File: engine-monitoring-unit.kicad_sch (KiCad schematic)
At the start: 58 parts, among them J1 Conn_01x04_Pin, J2 Supply, J3 Oil Temperature, J4 Air Temperature, J5 Air Temperature, J7 Inductive Sensor Wire, Q1 2N3904, SW1 KEY, SW2 RST, SW3 BOOT, U1 STM32F411CEU6, U2 LMR16006XDDCR, Y1 LSE, Y3 HSE

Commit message: Assigned Footprints for components
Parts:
- removed C5: C, symbol Device:C
- removed J7: Inductive Sensor Wire, TerminalBlock_Phoenix:TerminalBlock_Phoenix_MKDS-1,5-2-5.08_1x02_P5.08mm_Horizontal, symbol Connector:Screw_Terminal_01x02
- removed L1: L, symbol Device:L
- added C4: 100nF, Capacitor_SMD:C_0603_1608Metric_Pad1.08x0.95mm_HandSolder, symbol Device:C
- added J6: Sense Wire, Connector_Molex:Molex_Micro-Fit_3.0_43650-0200_1x02_P3.00mm_Horizontal, symbol Connector:Conn_01x02_Socket
- C1: renamed from C2; value C -> 4.7uF; footprint (none) -> Capacitor_SMD:C_0603_1608Metric_Pad1.08x0.95mm_HandSolder
- C10: renamed from C13; footprint (none) -> Capacitor_SMD:C_0603_1608Metric_Pad1.08x0.95mm_HandSolder
- C11: renamed from C9; value C -> 6.8pF; footprint (none) -> Capacitor_SMD:C_0603_1608Metric_Pad1.08x0.95mm_HandSolder
- C12: renamed from C15; footprint (none) -> Capacitor_SMD:C_0603_1608Metric_Pad1.08x0.95mm_HandSolder
- C13: renamed from C10; value C -> 6.8pF; footprint (none) -> Capacitor_SMD:C_0603_1608Metric_Pad1.08x0.95mm_HandSolder
- C14: renamed from C6; value C -> 4.7uF; footprint (none) -> Capacitor_SMD:C_0603_1608Metric_Pad1.08x0.95mm_HandSolder
- C15: renamed from C17; footprint (none) -> Capacitor_SMD:C_0603_1608Metric_Pad1.08x0.95mm_HandSolder
- C16: footprint (none) -> Capacitor_SMD:C_0603_1608Metric_Pad1.08x0.95mm_HandSolder
- C17: renamed from C14; footprint Capacitor_THT:CP_Radial_D8.0mm_P3.50mm -> Capacitor_SMD:C_0603_1608Metric_Pad1.08x0.95mm_HandSolder
- C2: renamed from C3; value C -> 100nF; footprint (none) -> Capacitor_SMD:C_0603_1608Metric_Pad1.08x0.95mm_HandSolder
- C3: renamed from C4; value C -> 100nF; footprint (none) -> Capacitor_SMD:C_0603_1608Metric_Pad1.08x0.95mm_HandSolder
- C5: renamed from C1; footprint (none) -> Capacitor_SMD:C_0603_1608Metric_Pad1.08x0.95mm_HandSolder
- C6: renamed from C7; value C -> 24pF; footprint (none) -> Capacitor_SMD:C_0603_1608Metric_Pad1.08x0.95mm_HandSolder
- C7: renamed from C11; footprint (none) -> Capacitor_SMD:C_0603_1608Metric_Pad1.08x0.95mm_HandSolder
- C8: renamed from C12; value 2.2uF -> 4.7uF; footprint (none) -> Capacitor_SMD:C_0603_1608Metric_Pad1.08x0.95mm_HandSolder
- C9: renamed from C8; value C -> 24pF; footprint (none) -> Capacitor_SMD:C_0603_1608Metric_Pad1.08x0.95mm_HandSolder
- D1: renamed from D2; footprint (none) -> LED_SMD:LED_0603_1608Metric_Pad1.05x0.95mm_HandSolder
- D2: renamed from D1; footprint (none) -> LED_SMD:LED_0603_1608Metric_Pad1.05x0.95mm_HandSolder
- J1: value Conn_01x04_Pin -> SW Debug; footprint (none) -> Connector_PinHeader_1.00mm:PinHeader_1x04_P1.00mm_Vertical
- J2, J3, J4: footprint (none) -> Connector_Molex:Molex_Micro-Fit_3.0_43650-0200_1x02_P3.00mm_Horizontal
- J5: value Air Temperature -> Wheel Speed; footprint (none) -> Connector_Molex:Molex_Micro-Fit_3.0_43650-0200_1x02_P3.00mm_Horizontal
- R1: renamed from R4; value R -> 1K; footprint (none) -> Resistor_SMD:R_0603_1608Metric_Pad0.98x0.95mm_HandSolder
- R10: renamed from R13; footprint (none) -> Resistor_SMD:R_0603_1608Metric_Pad0.98x0.95mm_HandSolder
- R11: renamed from R14; footprint (none) -> Resistor_SMD:R_0603_1608Metric_Pad0.98x0.95mm_HandSolder
- R13: renamed from R12; footprint Resistor_THT:R_Axial_DIN0207_L6.3mm_D2.5mm_P10.16mm_Horizontal -> Resistor_SMD:R_0603_1608Metric_Pad0.98x0.95mm_HandSolder
- R15: renamed from R10; footprint Resistor_THT:R_Axial_DIN0207_L6.3mm_D2.5mm_P10.16mm_Horizontal -> Resistor_SMD:R_0603_1608Metric_Pad0.98x0.95mm_HandSolder
- R16: renamed from R11; footprint Resistor_THT:R_Axial_DIN0207_L6.3mm_D2.5mm_P10.16mm_Horizontal -> Resistor_SMD:R_0603_1608Metric_Pad0.98x0.95mm_HandSolder
- R2: renamed from R3; footprint (none) -> Resistor_SMD:R_0603_1608Metric_Pad0.98x0.95mm_HandSolder
- R3: renamed from R2; footprint (none) -> Resistor_SMD:R_0603_1608Metric_Pad0.98x0.95mm_HandSolder
- R4: renamed from R5; value R -> 1K; footprint (none) -> Resistor_SMD:R_0603_1608Metric_Pad0.98x0.95mm_HandSolder
- R5: renamed from R1; footprint (none) -> Resistor_SMD:R_0603_1608Metric_Pad0.98x0.95mm_HandSolder
- R6, R7: footprint (none) -> Resistor_SMD:R_0603_1608Metric_Pad0.98x0.95mm_HandSolder
- R8: renamed from R9; footprint (none) -> Resistor_SMD:R_0603_1608Metric_Pad0.98x0.95mm_HandSolder
- R9: renamed from R8; footprint (none) -> Resistor_SMD:R_0603_1608Metric_Pad0.98x0.95mm_HandSolder
- SW1: footprint (none) -> Button_Switch_SMD:SW_Push_SPST_NO_Alps_SKRK
- SW2: renamed from SW3; footprint (none) -> Button_Switch_SMD:SW_Push_SPST_NO_Alps_SKRK
- SW3: renamed from SW2; footprint (none) -> Button_Switch_SMD:SW_Push_SPST_NO_Alps_SKRK
- renumbered D5 to D4, D4 to D5, L2 to L1, R18 to R12, R17 to R14, R15 to R17, R16 to R18, U2 to U1, U1 to U2, Y3 to Y1, Y1 to Y2
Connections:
- net +3.3V: now also C1.1, C2.1, C3.1, U2.9 (VDDA), C4.1
- net GND: now also C4.2, J6.2 (Pin_2)
- net at D5.2 (A), D7.1 (K): now also J6.1 (Pin_1)
- no-connect marks 0 -> 24
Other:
- note added: "0603"
- note added: "CAPS 0603/16v HSE - 8MHz LSE - 32.768KHz"
- note added: "DONE"
- moved on the sheet: C1, C3

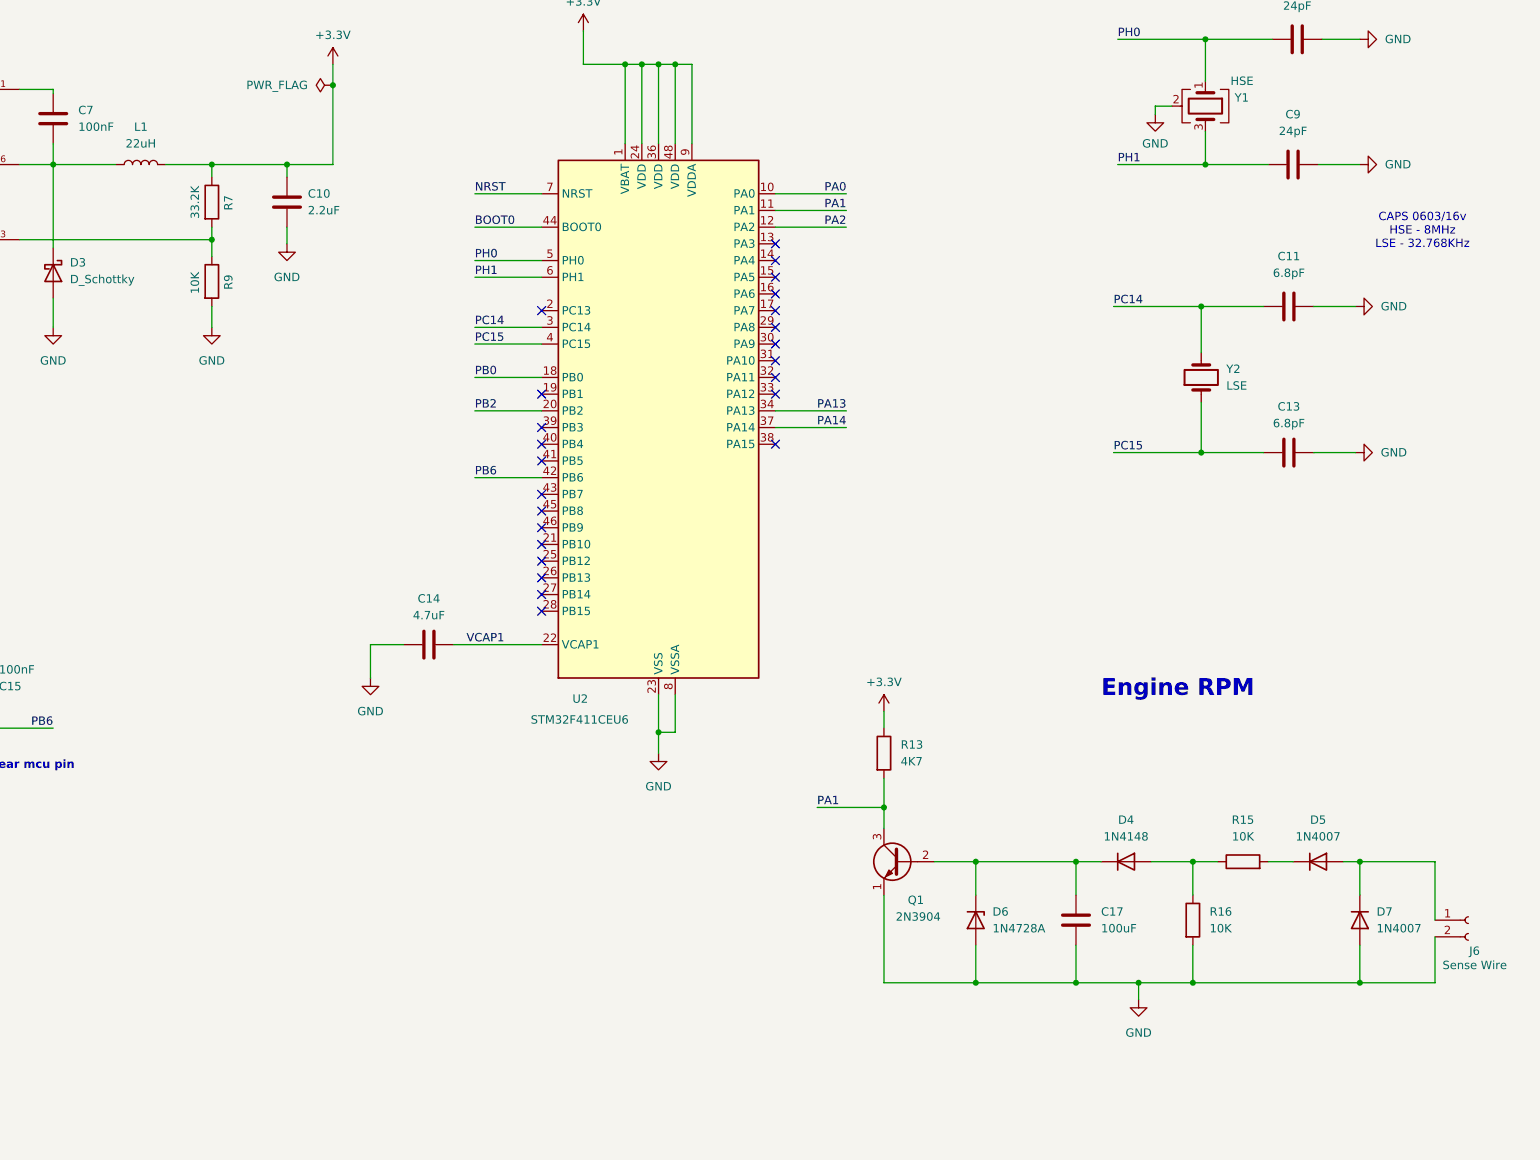
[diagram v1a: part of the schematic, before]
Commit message: Assigned 3D Models for missing ones
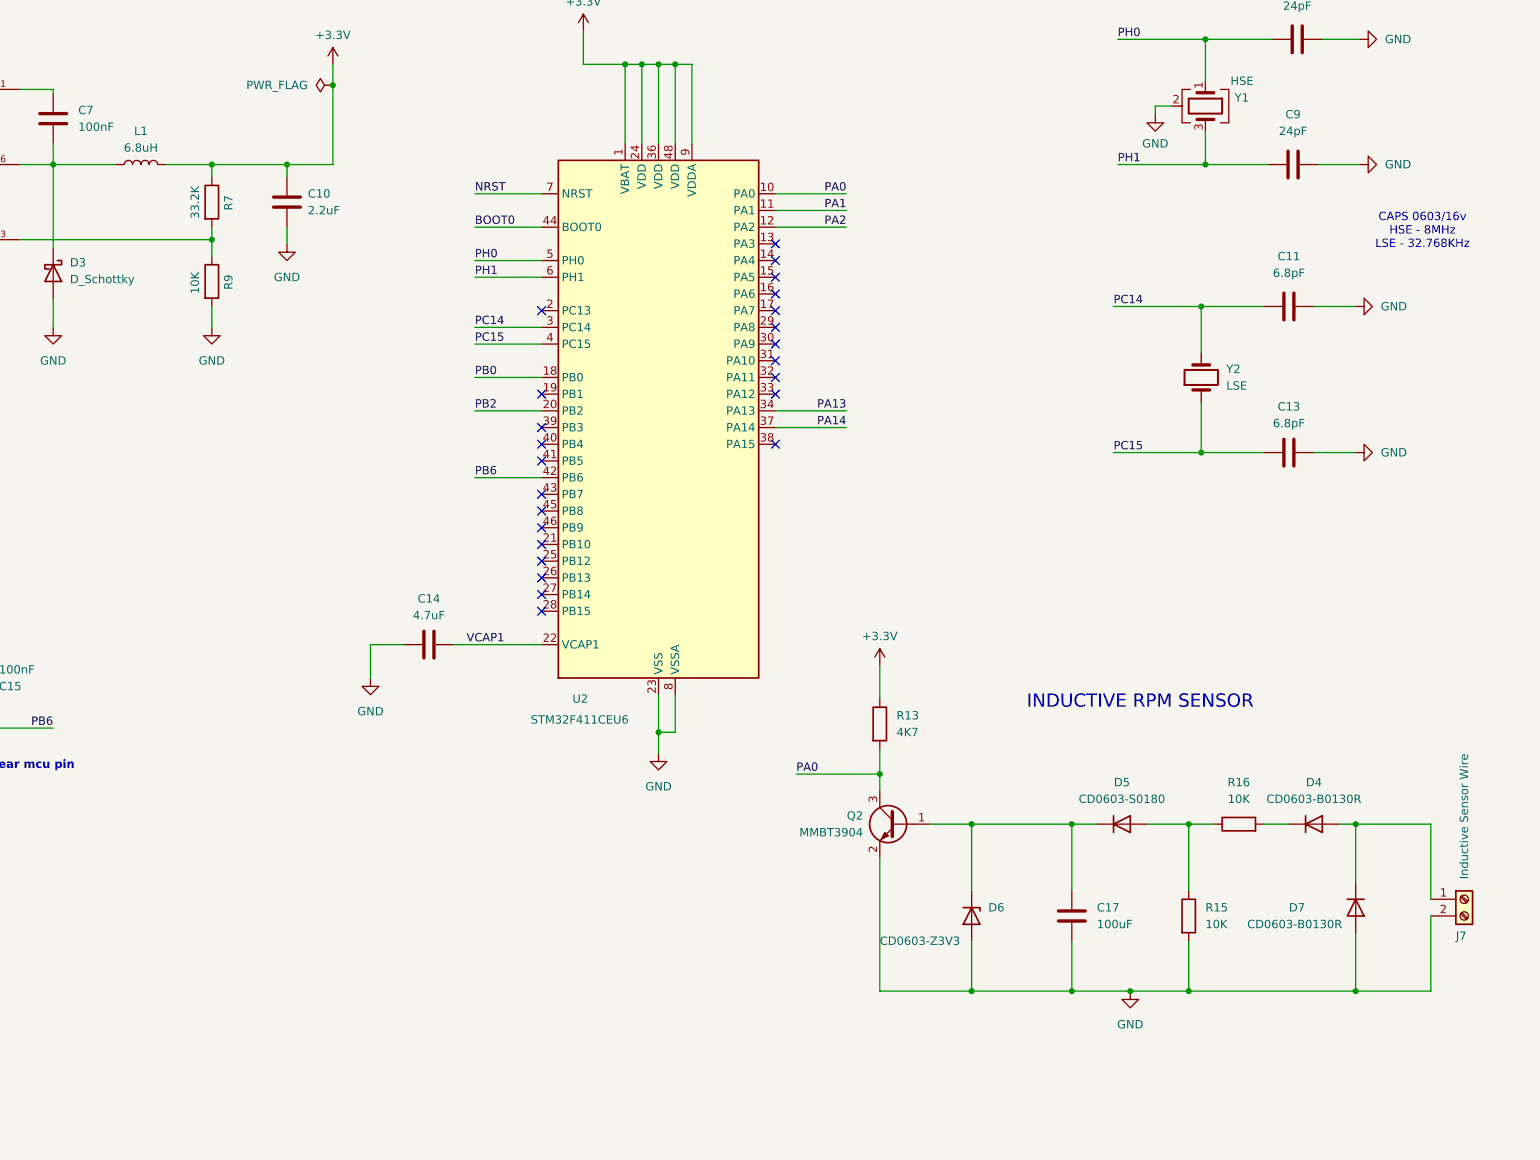
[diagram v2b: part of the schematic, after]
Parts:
- removed D4: 1N4148, Diode_THT:D_DO-35_SOD27_P7.62mm_Horizontal, symbol Diode:1N4148
- removed D5: 1N4007, Diode_THT:D_DO-41_SOD81_P10.16mm_Horizontal, symbol Diode:1N4007
- removed J6: Sense Wire, Connector_Molex:Molex_Micro-Fit_3.0_43650-0200_1x02_P3.00mm_Horizontal, symbol Connector:Conn_01x02_Socket
- removed Q1: 2N3904, Package_TO_SOT_THT:TO-92_Inline, symbol Transistor_BJT:2N3904
- added D4: CD0603-B0130R, Diode_SMD:D_0603_1608Metric_Pad1.05x0.95mm_HandSolder, symbol Diode:1N4007
- added D5: CD0603-S0180, Diode_SMD:D_0603_1608Metric_Pad1.05x0.95mm_HandSolder, symbol Diode:1N4148
- added J7: Inductive Sensor Wire, Connector_Molex:Molex_Micro-Fit_3.0_43650-0200_1x02_P3.00mm_Horizontal, symbol Connector:Screw_Terminal_01x02
- added Q2: MMBT3904, Package_TO_SOT_SMD:SOT-23, symbol Transistor_BJT:MMBT3904
- D3: footprint (none) -> Schottky:POWERDI-123_L2_8-W1_8-LS3_7-RD-1_SS14FP_C894423
- D6: value 1N4728A -> CD0603-Z3V3; footprint Diode_THT:D_DO-41_SOD81_P10.16mm_Horizontal -> Diode_SMD:D_0603_1608Metric_Pad1.05x0.95mm_HandSolder
- D7: value 1N4007 -> CD0603-B0130R; footprint Diode_THT:D_DO-41_SOD81_P10.16mm_Horizontal -> Diode_SMD:D_0603_1608Metric_Pad1.05x0.95mm_HandSolder
- L1: value 22uH -> 6.8uH; footprint (none) -> Inductor-6.8uH:IND-SMD_L4_0-W4_0_NRS4018T_NRS4018T6R8MDGJ_C222881
- R12, R14, R17, R18: footprint Resistor_THT:R_Axial_DIN0207_L6.3mm_D2.5mm_P10.16mm_Horizontal -> Resistor_SMD:R_0603_1608Metric_Pad0.98x0.95mm_HandSolder
- Y1: footprint (none) -> CRYSTAL-SMD_4P-L3_2-W2_5-BL_0132M4-8_000F16DTNJL_C19674293:CRYSTAL-SMD_4P-L3_2-W2_5-BL_0132M4-8_000F16DTNJL_C19674293
- Y2: footprint (none) -> lse:CRYSTAL-SMD_L3_2-W1_5-1_3131M32768DT06LL_C5221300
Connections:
- net GND: now also R15.2, J7.2 (Pin_2), Q2.2 (E); no longer R16.2
- net PA0: now also R13.2, Q2.3 (C)
- net PA1: no longer R13.2
- net at D7.1 (K): now also D4.2 (A), J7.1 (Pin_1)
- net at C17.1, D6.1 (K): now also D5.1 (K), Q2.1 (B)
- net at R15.1, R16.1: now also D5.2 (A)
- new net: D4.1 (K), R16.2
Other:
- note added: "INDUCTIVE RPM SENSOR"
- note removed: "Engine RPM"

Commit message: Updated Page Settings, Board Stackup and Constraints
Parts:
- renumbered D5 to D4, D4 to D5, D7 to D6, D6 to D7, J7 to J6, Q2 to Q1, R16 to R15, R15 to R16
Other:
- title: (none) -> Engine Monitoring Unit
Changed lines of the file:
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@@
 	(generator_version "10.0")
 	(paper "A3")
+	(title_block
+		(title "Engine Monitoring Unit")
+		(date "2026-08-05")
+		(rev "V1.0")
+		(comment 1 "Designed By - Harsha ")
+	)
 	(text "Indicator LEDs\n"
 		(exclude_from_sim no)
@@
 		)
 	)
+	(text "DONE\n"
+		(exclude_from_sim no)
+		(at 377.19 199.39 0)
+		(effects
+			(font
+				(size 1.27 1.27)
+				(thickness 0.254)
+				(bold yes)
+			)
+		)
+	)
 	(text "Place Cap near mcu pin\n"
 		(exclude_from_sim no)
@@
 		(effects
 			(font
-				(size 2.032 2.032)
+				(size 2.54 2.54)
+				(thickness 0.508)
+				(bold yes)
 			)
 		)
@@
 		(dnp no)
 		(fields_autoplaced yes)
-		(property "Reference" "#PWR041"
+		(property "Reference" "#PWR035"
 			(at 309.88 196.85 0)
 			(hide yes)
@@
 			(project "engine-monitoring-unit"
 				(path "/a9d3b11f-88d8-4654-952a-404ab772bc93"
-					(reference "#PWR041")
+					(reference "#PWR035")
 					(unit 1)
 				)
@@
 		(in_pos_files yes)
 		(dnp no)
-		(property "Reference" "Q2"
+		(property "Reference" "Q1"
 			(at 307.34 215.8999 0)
 			(show_name no)
@@
 			(project "engine-monitoring-unit"
 				(path "/a9d3b11f-88d8-4654-952a-404ab772bc93"
-					(reference "Q2")
+					(reference "Q1")
 					(unit 1)
 				)
@@
 		(in_pos_files yes)
 		(dnp no)
-		(property "Reference" "D7"
+		(property "Reference" "D6"
 			(at 372.11 229.8699 90)
 			(show_name no)
@@
 			(project "engine-monitoring-unit"
 				(path "/a9d3b11f-88d8-4654-952a-404ab772bc93"
-					(reference "D7")
+					(reference "D6")
 					(unit 1)
 				)
@@
 		(dnp no)
 		(fields_autoplaced yes)
-		(property "Reference" "#PWR036"
+		(property "Reference" "#PWR041"
 			(at 347.98 248.92 0)
 			(hide yes)
@@
 			(project "engine-monitoring-unit"
 				(path "/a9d3b11f-88d8-4654-952a-404ab772bc93"
-					(reference "#PWR036")
+					(reference "#PWR041")
 					(unit 1)
 				)
@@
 		(dnp no)
 		(fields_autoplaced yes)
-		(property "Reference" "D5"
+		(property "Reference" "D4"
 			(at 346.71 210.82 0)
 			(show_name no)
@@
 			(project "engine-monitoring-unit"
 				(path "/a9d3b11f-88d8-4654-952a-404ab772bc93"
-					(reference "D5")
+					(reference "D4")
 					(unit 1)
 				)
@@
 		(in_pos_files yes)
 		(dnp no)
-		(property "Reference" "D6"
+		(property "Reference" "D7"
 			(at 326.39 229.8699 90)
 			(show_name no)
@@
 			(project "engine-monitoring-unit"
 				(path "/a9d3b11f-88d8-4654-952a-404ab772bc93"
-					(reference "D6")
+					(reference "D7")
 					(unit 1)
 				)
@@
 		(dnp no)
 		(fields_autoplaced yes)
-		(property "Reference" "#PWR035"
+		(property "Reference" "#PWR036"
 			(at 232.41 201.295 0)
 			(hide yes)
@@
 			(project "engine-monitoring-unit"
 				(path "/a9d3b11f-88d8-4654-952a-404ab772bc93"
-					(reference "#PWR035")
+					(reference "#PWR036")
 					(unit 1)
 				)
@@
 		(dnp no)
 		(fields_autoplaced yes)
-		(property "Reference" "R15"
+		(property "Reference" "R16"
 			(at 359.41 229.8699 0)
 			(show_name no)
@@
 			(project "engine-monitoring-unit"
 				(path "/a9d3b11f-88d8-4654-952a-404ab772bc93"
-					(reference "R15")
+					(reference "R16")
 					(unit 1)
 				)
@@
 		(dnp no)
 		(fields_autoplaced yes)
-		(property "Reference" "D4"
+		(property "Reference" "D5"
 			(at 375.92 210.82 0)
 			(show_name no)
@@
 			(project "engine-monitoring-unit"
 				(path "/a9d3b11f-88d8-4654-952a-404ab772bc93"
-					(reference "D4")
+					(reference "D5")
 					(unit 1)
 				)
@@
 		(dnp no)
 		(fields_autoplaced yes)
-		(property "Reference" "R16"
+		(property "Reference" "R15"
 			(at 364.49 210.82 90)
 			(show_name no)
@@
 			(project "engine-monitoring-unit"
 				(path "/a9d3b11f-88d8-4654-952a-404ab772bc93"
-					(reference "R16")
+					(reference "R15")
 					(unit 1)
 				)
@@
 		(in_pos_files yes)
 		(dnp no)
-		(property "Reference" "J7"
+		(property "Reference" "J6"
 			(at 397.51 234.188 0)
 			(show_name no)
@@
 			(project "engine-monitoring-unit"
 				(path "/a9d3b11f-88d8-4654-952a-404ab772bc93"
-					(reference "J7")
+					(reference "J6")
 					(unit 1)
 				)

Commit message: Layed out decoupling caps, connectors and switches
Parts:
- removed C14: 4.7uF, Capacitor_SMD:C_0603_1608Metric_Pad1.08x0.95mm_HandSolder, symbol Device:C
- added C1, C6, C7: 100nF, Capacitor_SMD:C_0603_1608Metric_Pad1.08x0.95mm_HandSolder, symbol Device:C
- added C17: 4.7uF, Capacitor_SMD:C_0603_1608Metric_Pad1.08x0.95mm_HandSolder, symbol Device:C
- D1: value LED_PWR -> LED_USER
- D2: value LED_USER -> LED_PWR
- renumbered C7 to C10, C8 to C11, C9 to C12, C10 to C13, C11 to C14, C12 to C15, C13 to C16, C15 to C18, C16 to C19, C1 to C2, C17 to C20, C2 to C3, C3 to C4, C4 to C5, C5 to C8, C6 to C9
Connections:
- net +3.3V: now also C6.1, C7.1
- net GND: now also C1.1, C17.1, C6.2, C7.2
- net PA0: now also C1.2
- net PA3: now also U2.13 (PA3)
- net PC13: now also U2.2 (PC13)
- net VCAP1: now also C17.2
- net PA1: no longer names the net of U2.11 (PA1)
- no-connect marks 24 -> 23

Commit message: Routed Signal Traces
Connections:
- net PA0: no longer C1.2, SW1.1
- net PA11: now reaches U2.32 (PA11)
- net PA11: now also C1.2, SW1.1
- no-connect marks 23 -> 22
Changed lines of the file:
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@@
+	)
+	(junction
+		(at 234.95 49.53)
+		(diameter 0)
+		(color 0 0 0 0)
+	)
+	(junction
+		(at 141.605 105.41)
+		(diameter 0)
+		(color 0 0 0 0)
+	)
+	(junction
+		(at 182.88 50.165)
+		(diameter 0)
+		(color 0 0 0 0)
 	)
 	(junction
@@
 	)
 	(junction
-		(at 234.95 49.53)
-		(diameter 0)
-		(color 0 0 0 0)
-	)
-	(junction
-		(at 141.605 105.41)
-		(diameter 0)
-		(color 0 0 0 0)
-	)
-	(junction
-		(at 182.88 50.165)
-		(diameter 0)
-		(color 0 0 0 0)
-	)
-	(junction
 		(at 123.19 100.965)
 		(diameter 0)
@@
 		(diameter 0)
 		(color 0 0 0 0)
-	)
-	(no_connect
-		(at 297.18 148.59)
 	)
 	(no_connect
@@
 	(wire
 		(pts
+			(xy 297.18 148.59) (xy 307.34 148.59)
+		)
+		(stroke
+			(width 0)
+			(type default)
+		)
+	)
+	(wire
+		(pts
 			(xy 141.605 114.3) (xy 141.605 116.84)
 		)
@@
 	(wire
 		(pts
+			(xy 31.75 34.29) (xy 36.83 34.29)
+		)
+		(stroke
+			(width 0)
+			(type default)
+		)
+	)
+	(wire
+		(pts
 			(xy 375.92 160.655) (xy 382.27 160.655)
 		)
@@
 		(pts
 			(xy 267.97 95.885) (xy 267.97 100.965)
-		)
-		(stroke
-			(width 0)
-			(type default)
-		)
-	)
-	(wire
-		(pts
-			(xy 33.655 34.29) (xy 36.83 34.29)
 		)
 		(stroke
@@
 		)
 	)
+	(label "PA11"
+		(at 31.75 34.29 180)
+		(effects
+			(font
+				(size 1.27 1.27)
+				(thickness 0.1588)
+			)
+			(justify right bottom)
+		)
+	)
 	(label "PA2"
 		(at 307.975 125.73 180)
@@
 		)
 	)
-	(label "PA0"
-		(at 33.655 34.29 0)
+	(label "PA11"
+		(at 307.34 148.59 180)
 		(effects
 			(font
 				(size 1.27 1.27)
+				(thickness 0.1588)
 			)
-			(justify left bottom)
-		)
-	)
+			(justify right bottom)
+		)
+	)

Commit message: Updated Footprint for swd
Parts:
- J1: footprint Connector_PinHeader_1.00mm:PinHeader_1x04_P1.00mm_Vertical -> Connector_PinHeader_2.54mm:PinHeader_1x04_P2.54mm_Vertical
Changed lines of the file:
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@@
 			)
 		)
-		(property "Footprint" "Connector_PinHeader_1.00mm:PinHeader_1x04_P1.00mm_Vertical"
+		(property "Footprint" "Connector_PinHeader_2.54mm:PinHeader_1x04_P2.54mm_Vertical"
 			(at 365.76 46.99 0)
 			(hide yes)

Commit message: Added OLED Display Socket
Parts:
- added J7: SW Debug, Connector_PinSocket_2.54mm:PinSocket_1x04_P2.54mm_Vertical, symbol Connector:Conn_01x04_Pin
- added R19, R20: 2.2K, Resistor_SMD:R_0603_1608Metric_Pad0.98x0.95mm_HandSolder, symbol Device:R
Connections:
- net +3.3V: now also J7.1 (Pin_1), R19.1, R20.1
- net GND: now also J7.4 (Pin_4)
- net PB10: now reaches U2.21 (PB10)
- net PB10: now also J7.3 (Pin_3), R20.2
- net PB3: now reaches U2.39 (PB3)
- net PB3: now also J7.2 (Pin_2), R19.2
- no-connect marks 22 -> 20
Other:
- note added: "Oled Display Connector"
